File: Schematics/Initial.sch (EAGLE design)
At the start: 31 parts, among them J1 AVR_SPI_PRG, U1 ATMEGA32U4, U2 3.3V_REG_LDOSMD, X1 USBSMD, Y1 16MHz

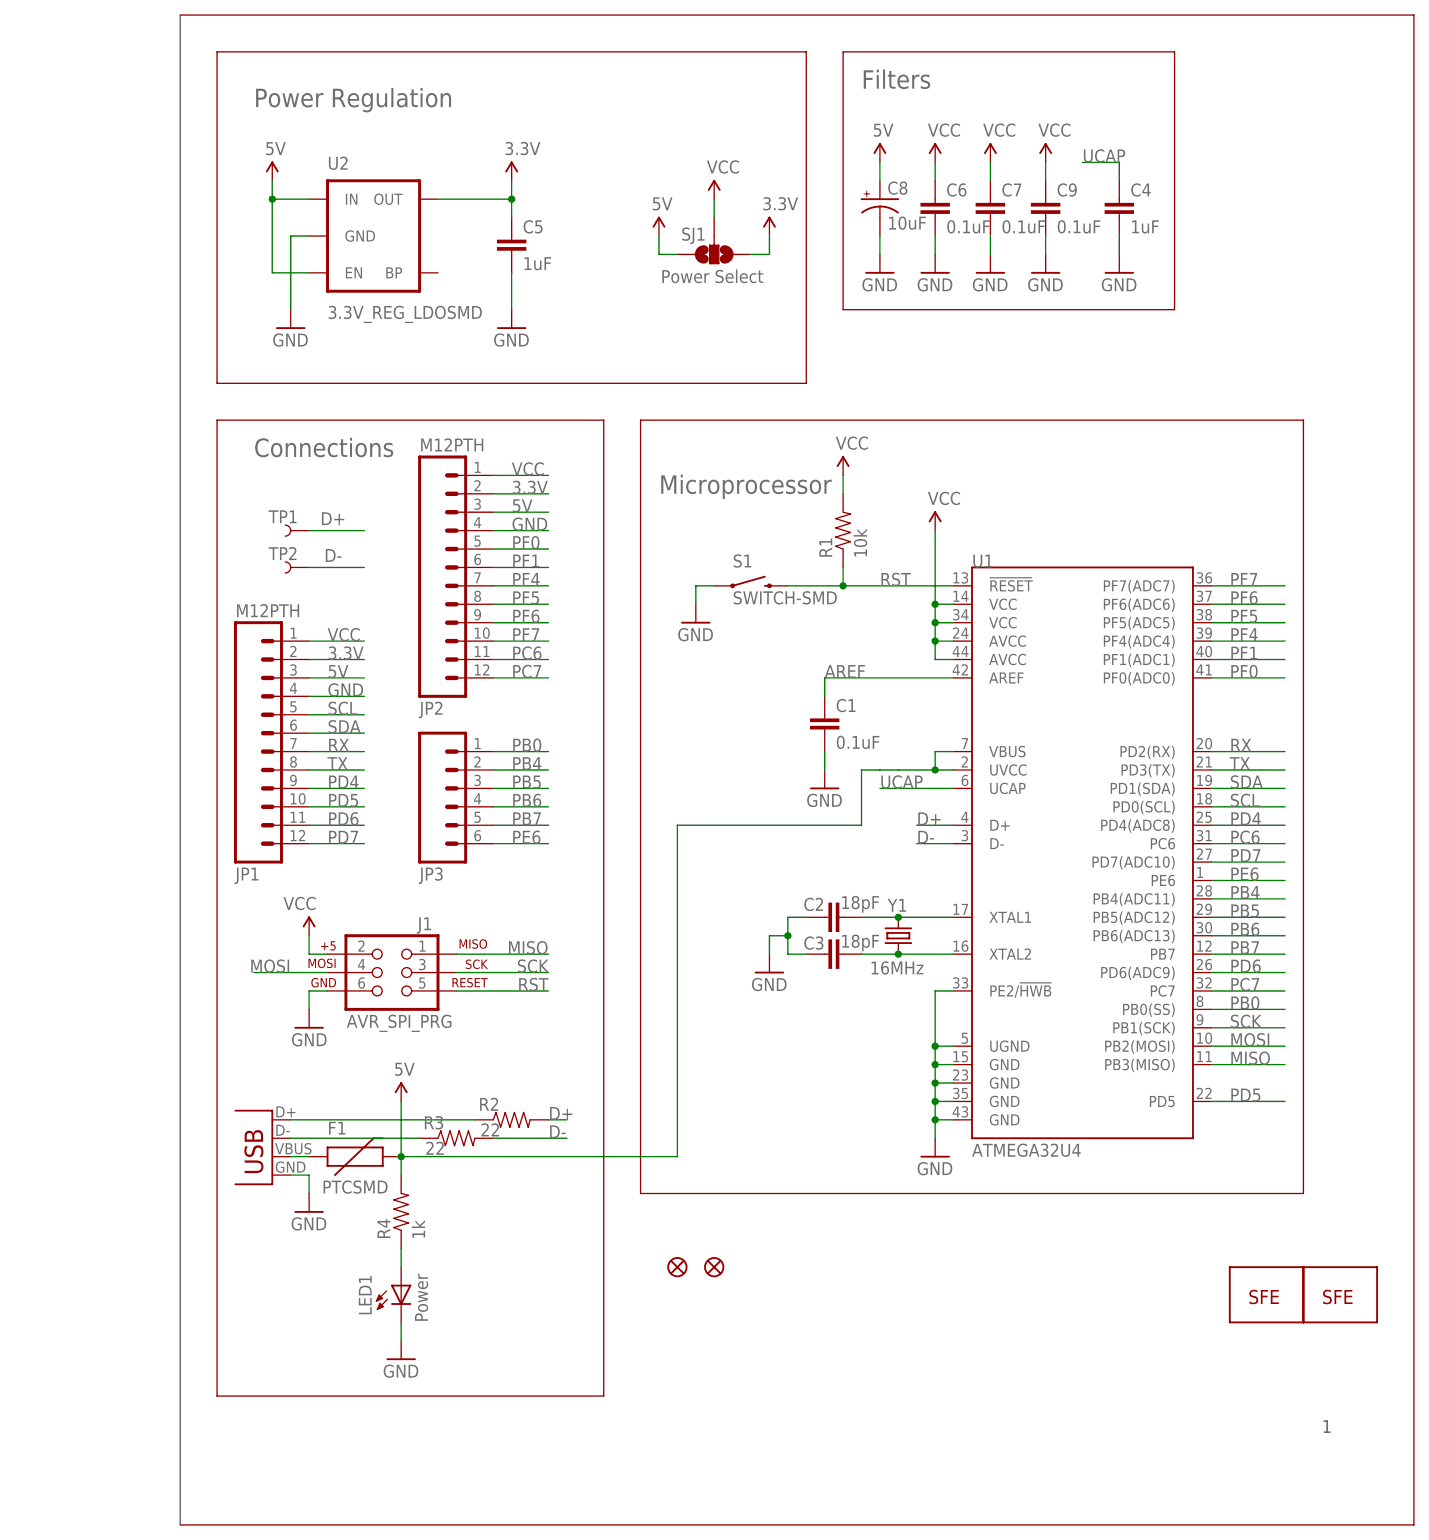
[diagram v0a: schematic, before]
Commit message: Changed package types for passives
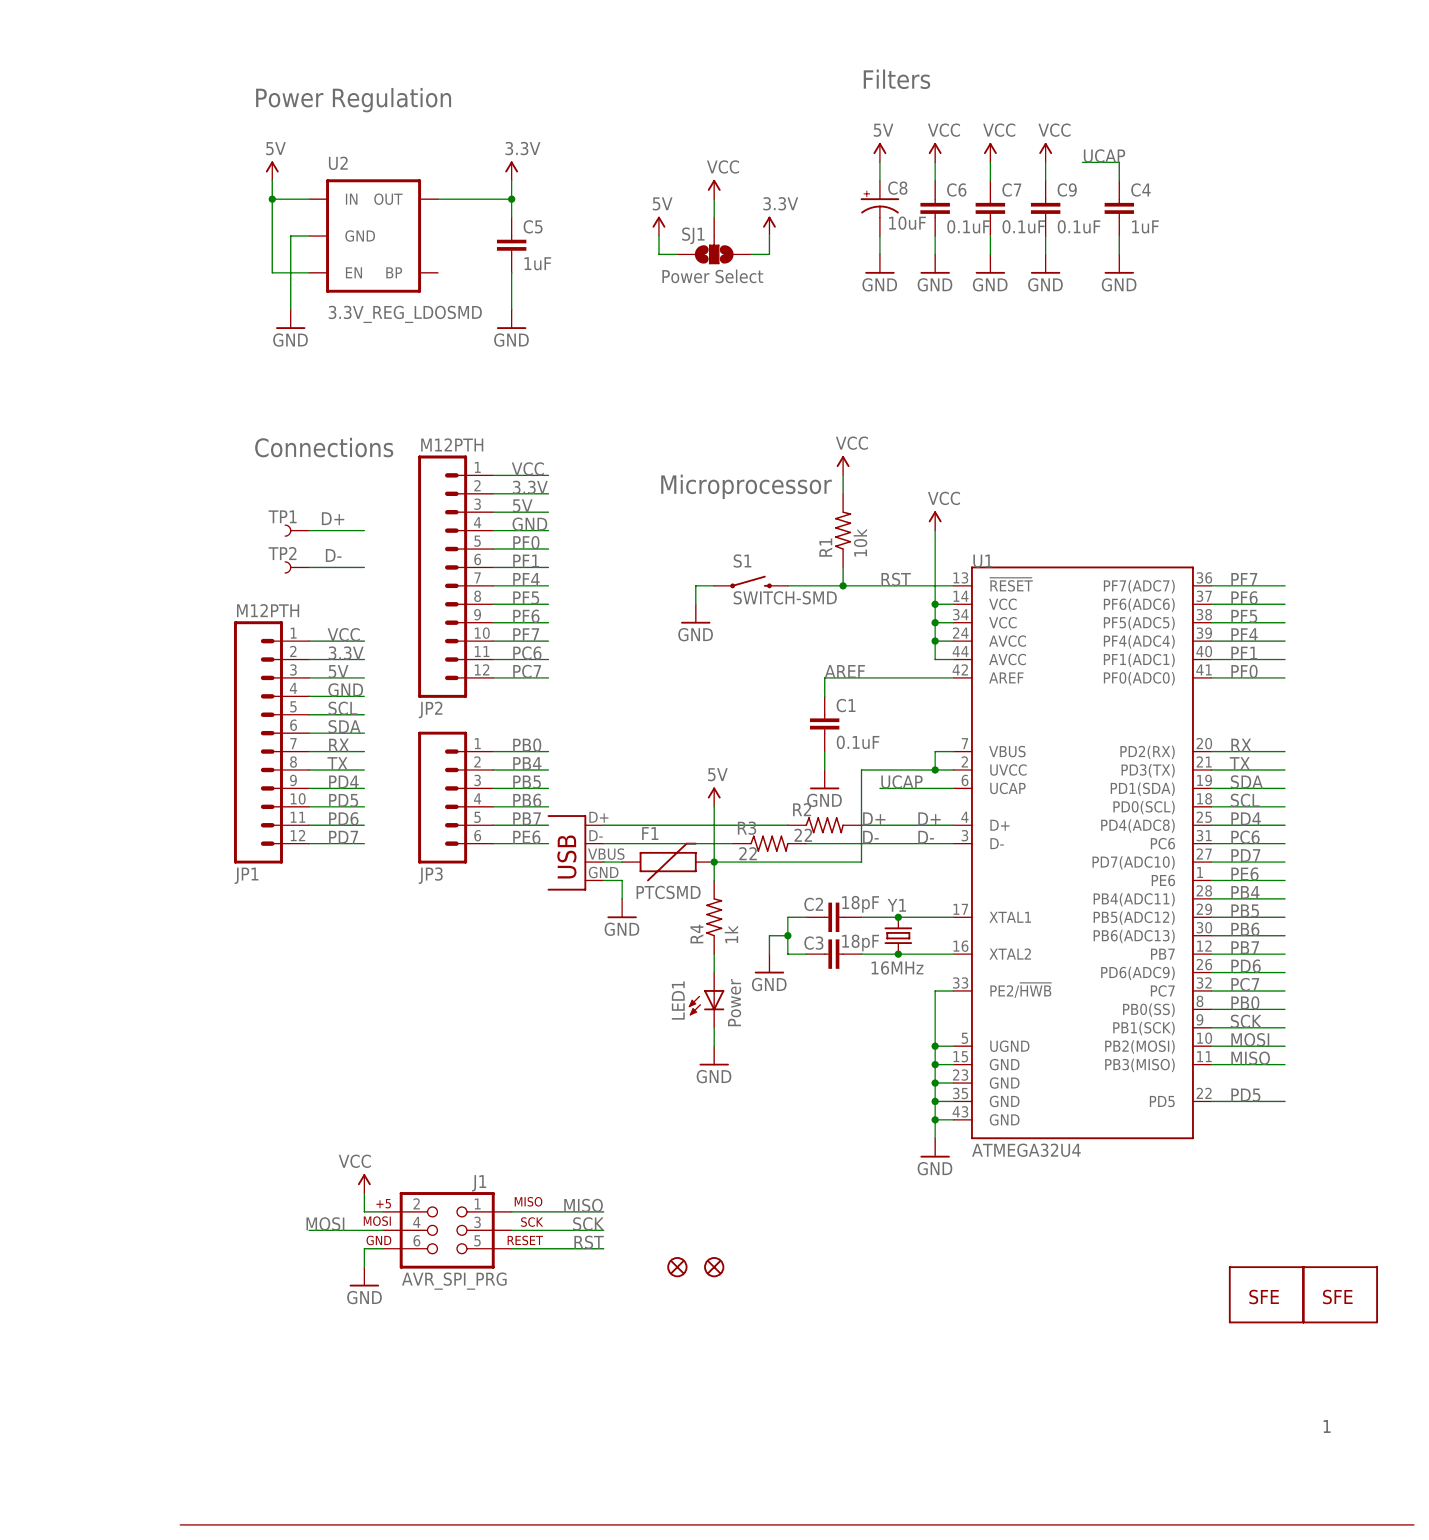
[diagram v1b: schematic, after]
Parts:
- C1, C2, C3: device SparkFun:CAP0402-CAP -> SparkFun:CAP0805
- R1, R2, R3, R4: device SparkFun:RESISTOR0402-RES -> resistor:R-US_M0805
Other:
- moved on the sheet: F1, J1, LED1, R2, R3, R4

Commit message: Schematic w/PMIC
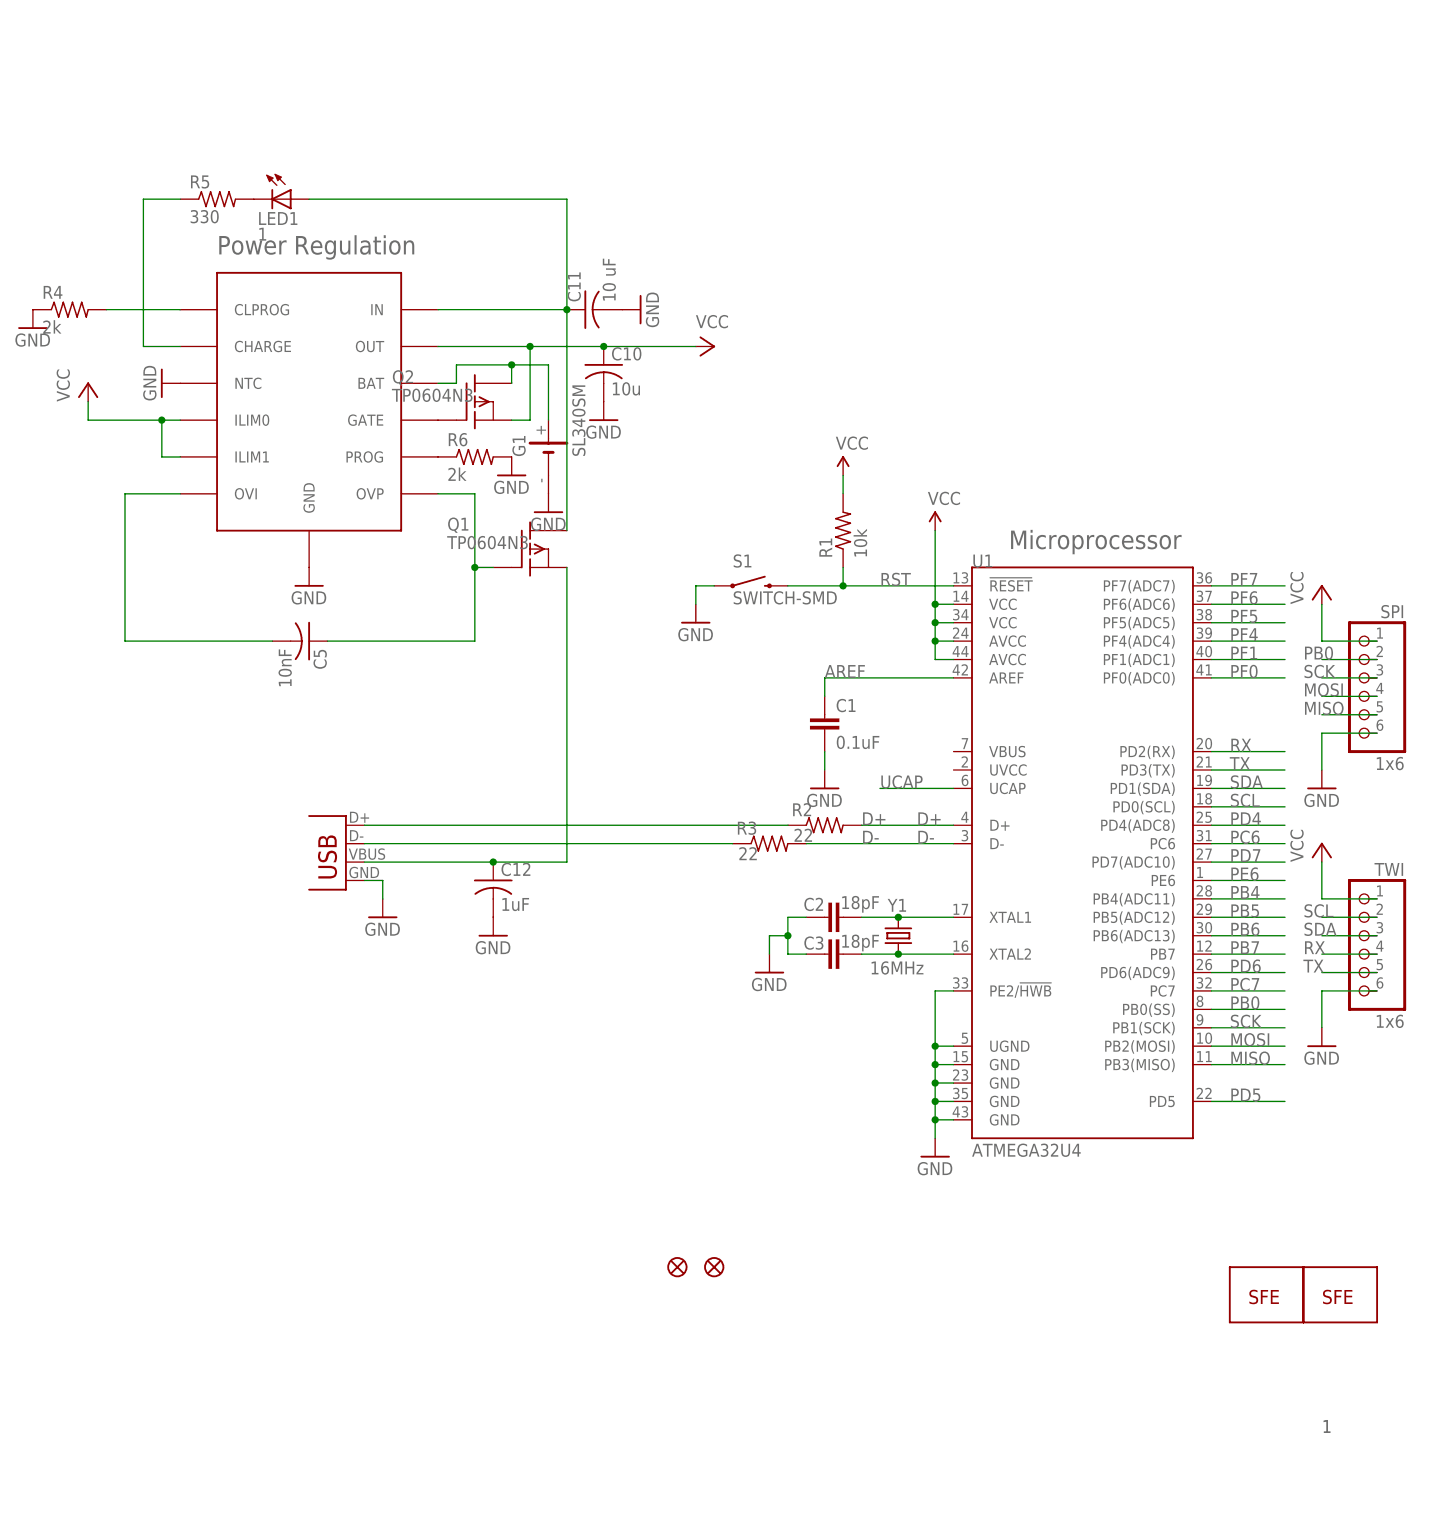
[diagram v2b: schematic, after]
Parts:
- removed C4: 1uF, SparkFun:CAP0402-CAP
- removed C6, C7, C9: 0.1uF, SparkFun:CAP0402-CAP
- removed C8: 10uF, SparkFun:CAP_POL1206
- removed F1: PTCSMD, SparkFun:PTCSMD
- removed J1: AVR_SPI_PRG, SparkFun:AVR_SPI_PRG_6PTH
- removed JP1, JP2: M12PTH, SparkFun:M12PTH
- removed JP3: (no value), SparkFun:M06SIP
- removed SJ1: Power Select, SparkFun:SOLDERJUMPER_2WAYPASTE2&3
- removed TP1, TP2: TEST-POINT3, SparkFun:TEST-POINT3
- removed U2: 3.3V_REG_LDOSMD, SparkFun:V_REG_LDOSMD
- added C10: 10u, rcl:C-USC0805
- added C11: 10 uF, rcl:C-USC0805
- added C12: 1uF, rcl:C-USC0805
- added G1: SL340SM, battery:SL340SM
- added LTC4067: LTC4067, LTC4067:LTC4067
- added Q1, Q2: TP0604N3, transistor-fet:TP0604N3
- added R5: 330, resistor:R-US_M0805
- added R6: 2k, resistor:R-US_M0805
- added SPI, TWI: 1x6, pinhead:PINHD-1X6
- C5: value 1uF -> 10nF; device SparkFun:CAP0402-CAP -> rcl:C-USC0805
- LED1: value Power -> 1; device SparkFun:LED0603 -> led:LEDCHIPLED_0805
- R4: value 1k -> 2k
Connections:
- removed net 3.3V: C5.1, JP1.2, JP2.2, SJ1.1, U2.OUT
- removed net 5V: C8.+, JP1.3, JP2.3, SJ1.3, U2.EN, U2.IN
- removed net VBUS: F1.2, R4.2, U1.UVCC, U1.VBUS
- new net N$1: C5.1, LTC4067.OVP, Q1.G
- new net N$10: C12.1, Q1.S, X1.VBUS
- new net N$11: LTC4067.GATE, Q2.G
- new net N$12: R3.1, X1.D-
- new net N$13: R2.1, X1.D+
- new net N$16: C5.2, LTC4067.OVI
- new net N$5: G1.+, LTC4067.BAT, Q2.D
- new net N$6: LTC4067.CLPROG, R4.2
- new net N$7: LTC4067.CHARGE, R5.1
- new net N$8: LED1.C, R5.2
- net D+: no longer R2.1, TP1.1, X1.D+
- net D-: no longer R3.1, TP2.1, X1.D-
- net GND: now also C10.2, C11.2, C12.2, G1.-, LTC4067.GND, LTC4067.NTC, R4.1, R6.2, SPI.6, TWI.6; no longer C4.2, C5.2, C6.2, C7.2, C8.-, C9.2, J1.6, JP1.4, JP2.4, LED1.C, U2.GND
- net MISO: now also SPI.5; no longer J1.1
- net MOSI: now also SPI.4; no longer J1.4
- net N$4: now also LTC4067.PROG, R6.1; no longer F1.1, X1.VBUS
- net N$9: now also C11.1, LTC4067.IN, Q1.D; no longer R4.1
- net PB0: now also SPI.2; no longer JP3.1
- net PB4: no longer JP3.2
- net PB5: no longer JP3.3
- net PB6: no longer JP3.4
- net PB7: no longer JP3.5
- net PC6: no longer JP2.11
- net PC7: no longer JP2.12
- net PD4: no longer JP1.9
- net PD5: no longer JP1.10
- net PD6: no longer JP1.11
- net PD7: no longer JP1.12
- net PE6: no longer JP3.6
- net PF0: no longer JP2.5
- net PF1: no longer JP2.6
- net PF4: no longer JP2.7
- net PF5: no longer JP2.8
- net PF6: no longer JP2.9
- net PF7: no longer JP2.10
- net RST: no longer J1.5
- net RX: now also TWI.4; no longer JP1.7
- net SCK: now also SPI.3; no longer J1.3
- net SCL: now also TWI.2; no longer JP1.5
- net SDA: now also TWI.3; no longer JP1.6
- net TX: now also TWI.5; no longer JP1.8
- net UCAP: no longer C4.1
- net VCC: now also C10.1, LTC4067.ILIM0, LTC4067.ILIM1, LTC4067.OUT, Q2.S, SPI.1, TWI.1; no longer C6.1, C7.1, C9.1, J1.2, JP1.1, JP2.1, SJ1.2
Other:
- note removed: "Connections"
- note removed: "Filters"
- moved on the sheet: C5, LED1, R4
